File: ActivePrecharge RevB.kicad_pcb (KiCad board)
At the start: 2 copper layers, 98.4 x 58.9 mm, 78 parts, among them IC1 AMC1350DWVR, IC2 AMC1350DWVR, IC4 MCP6496UT-E_LT, IC5 MCP6496UT-E_LT, J1 HVConnector, J2 ExportConnector, J3 PrechargeContactor, J4 MainContactor, J5 Conn_01x07_Pin, U1 LT1963AEST-3.3#TRPBF

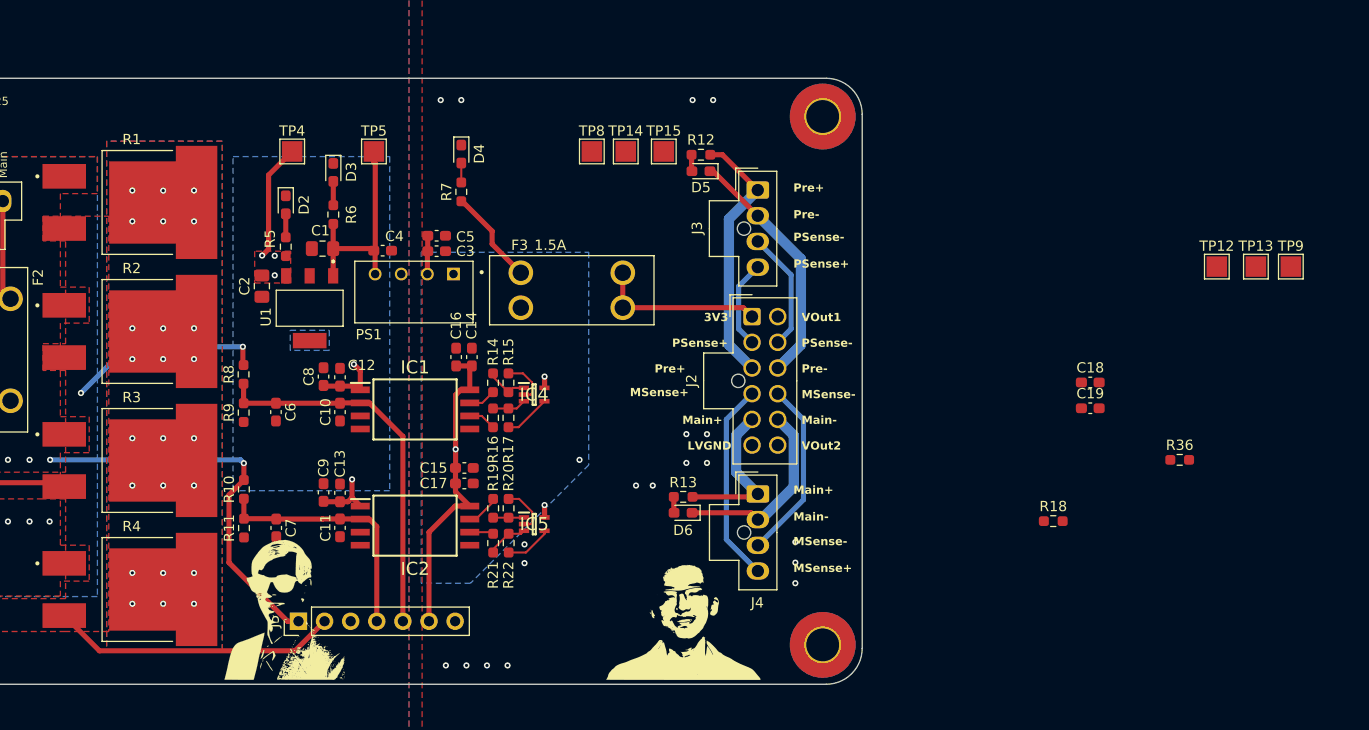
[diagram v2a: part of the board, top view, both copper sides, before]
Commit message: Did some of the initial layout after schematic changes, concerned about the choking on how i currently have the opamp kind of set up, also havent touched the testpoints yet so that will probably make it more complex
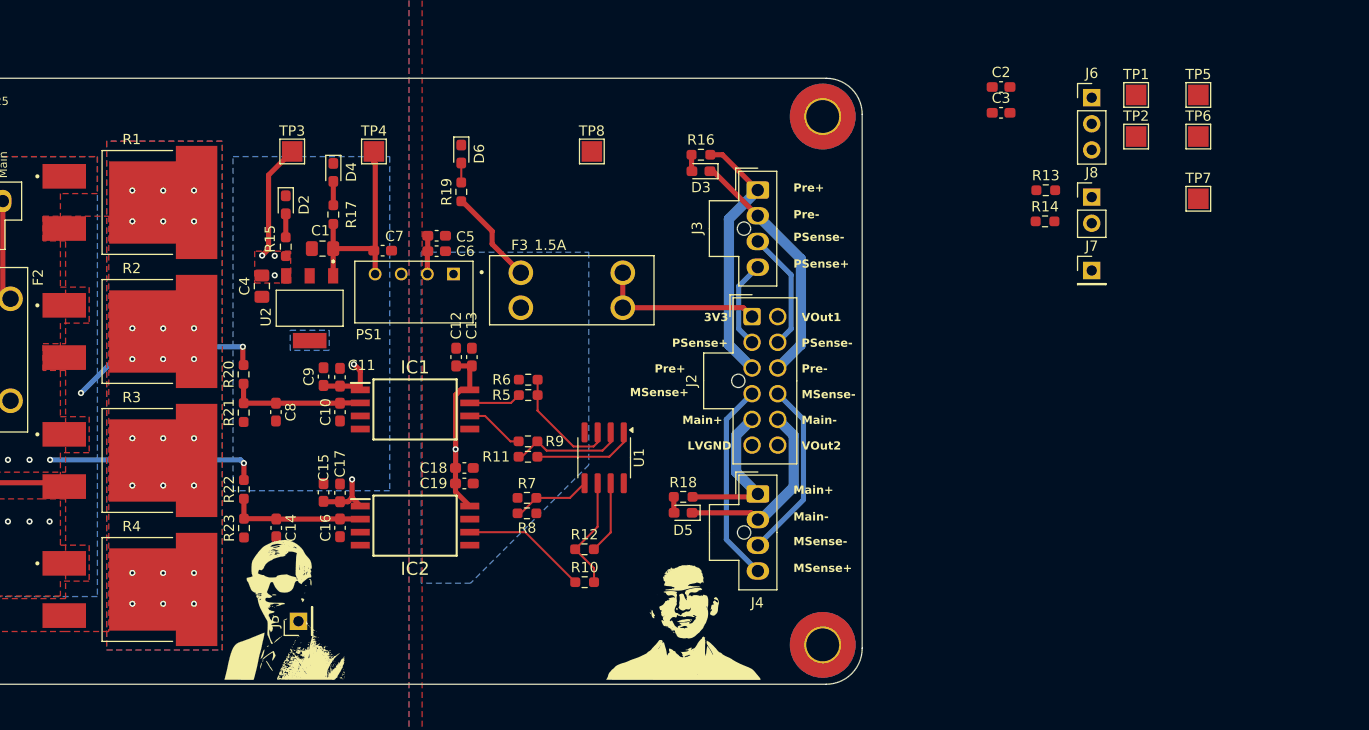
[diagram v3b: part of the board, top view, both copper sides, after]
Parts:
- removed the C18 at (220.7, 89.5)
- removed the C19 at (220.7, 92.0)
- removed IC4, IC5: MCP6496UT-E_LT, ActivePrecharge-RevB:SOT65P210X110-5N
- removed the R15 at (164.1, 89.5)
- removed the R16 at (162.6, 92.9)
- removed the R17 at (164.1, 92.9)
- removed the R18 at (217.1, 103.0)
- removed the R19 at (162.6, 101.7)
- removed the R20 at (164.1, 101.7)
- removed the R21 at (162.6, 105.1)
- removed the R22 at (164.1, 105.1)
- removed R36: 23, Resistor_SMD:R_0603_1608Metric_Pad0.98x0.95mm_HandSolder
- removed TP12: V1-, TestPoint:TestPoint_Pad_2.0x2.0mm
- removed TP13: V2-, TestPoint:TestPoint_Pad_2.0x2.0mm
- removed TP14: VOut1, TestPoint:TestPoint_Pad_2.0x2.0mm
- removed TP15: VOut2, TestPoint:TestPoint_Pad_2.0x2.0mm
- removed TP9: V2+, TestPoint:TestPoint_Pad_2.0x2.0mm
- added C2: 10nF, Capacitor_SMD:C_0603_1608Metric_Pad1.08x0.95mm_HandSolder, F.Cu at (212.0, 60.7)
- added C3: 10nF, Capacitor_SMD:C_0603_1608Metric_Pad1.08x0.95mm_HandSolder, F.Cu at (212.0, 63.2)
- added J6: Conn_01x03_Pin, Connector_PinHeader_2.54mm:PinHeader_1x03_P2.54mm_Vertical, F.Cu at (220.8, 61.8)
- added J7: Conn_01x01_Pin, Connector_PinHeader_2.54mm:PinHeader_1x01_P2.54mm_Vertical, F.Cu at (220.8, 78.6)
- added J8: Conn_01x02_Pin, Connector_PinHeader_2.54mm:PinHeader_1x02_P2.54mm_Vertical, F.Cu at (220.8, 71.4)
- added R10: 10k, Resistor_SMD:R_0603_1608Metric_Pad0.98x0.95mm_HandSolder, F.Cu at (171.5, 108.9)
- added R11: 10k, Resistor_SMD:R_0603_1608Metric_Pad0.98x0.95mm_HandSolder, F.Cu at (166.0, 96.7)
- added R12: 10k, Resistor_SMD:R_0603_1608Metric_Pad0.98x0.95mm_HandSolder, F.Cu at (171.5, 105.7)
- added R13: 10, Resistor_SMD:R_0603_1608Metric_Pad0.98x0.95mm_HandSolder, F.Cu at (216.4, 70.8)
- added R5: 10k, Resistor_SMD:R_0603_1608Metric_Pad0.98x0.95mm_HandSolder, F.Cu at (166.0, 90.7)
- added R6: 10k, Resistor_SMD:R_0603_1608Metric_Pad0.98x0.95mm_HandSolder, F.Cu at (166.0, 89.2)
- added R7: 10k, Resistor_SMD:R_0603_1608Metric_Pad0.98x0.95mm_HandSolder, F.Cu at (165.9, 100.7)
- added R8: 10k, Resistor_SMD:R_0603_1608Metric_Pad0.98x0.95mm_HandSolder, F.Cu at (165.9, 102.2)
- added R9: 10k, Resistor_SMD:R_0603_1608Metric_Pad0.98x0.95mm_HandSolder, F.Cu at (166.0, 95.2)
- added TP1: VOut1, TestPoint:TestPoint_Pad_2.0x2.0mm, F.Cu at (225.2, 61.5)
- added TP2: VOut2, TestPoint:TestPoint_Pad_2.0x2.0mm, F.Cu at (225.2, 65.5)
- added TP5: V+, TestPoint:TestPoint_Pad_2.0x2.0mm, F.Cu at (231.2, 61.5)
- added TP6: V-, TestPoint:TestPoint_Pad_2.0x2.0mm, F.Cu at (231.2, 65.5)
- added TP7: V+, TestPoint:TestPoint_Pad_2.0x2.0mm, F.Cu at (231.2, 71.6)
- added U1: TLV9002QDRQ1, Package_SO:SOIC-8_3.9x4.9mm_P1.27mm, F.Cu at (173.4, 96.8)
- C12: renamed from C16; value 100nF -> 1uF
- C13: renamed from C14; value 1uF -> 100nF
- J5: value Conn_01x07_Pin -> Conn_01x01_Pin; footprint Connector_PinHeader_2.54mm:PinHeader_1x07_P2.54mm_Vertical -> Connector_PinHeader_2.54mm:PinHeader_1x01_P2.54mm_Vertical
- R14: value 20k -> 10
- R16: renamed from R12; value 1k -> 10k
- R18: renamed from R13; value 1k -> 10k
- TP8: value V1+ -> V-
- moved R14 55.9 mm to (216.3, 73.8), turned to 0 degrees
- renumbered C12 to C11, C7 to C14, C9 to C15, C11 to C16, C13 to C17, C15 to C18, C17 to C19, C2 to C4, C3 to C6, C4 to C7, C6 to C8, C8 to C9, D5 to D3, D3 to D4, D6 to D5, D4 to D6, R5 to R15, R6 to R17, R7 to R19, R8 to R20, R9 to R21, R10 to R22, R11 to R23, TP4 to TP3, TP5 to TP4, U1 to U2
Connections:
- C10 pad 1: /Voltage_Sense/Vin1 -> /Vin1
- C14 pad 1: /Voltage_Sense/Vin2 -> /Vin2
- C16 pad 1: /Voltage_Sense/Vin2 -> /Vin2
- C8 pad 1: /Voltage_Sense/Vin1 -> /Vin1
- IC1 pad 2: /Voltage_Sense/Vin1 -> /Vin1
- IC1 pad 6: /Voltage_Sense/V1- -> /V1-
- IC1 pad 7: /Voltage_Sense/V1+ -> /V1+
- IC2 pad 2: /Voltage_Sense/Vin2 -> /Vin2
- IC2 pad 6: /Voltage_Sense/V2- -> /V2-
- IC2 pad 7: /Voltage_Sense/V2+ -> /V2+
- J5 pad 1: HV- -> HV+
- R14 pad 1: Net-(IC4-VIN+) -> /VOut2
- R14 pad 2: /Voltage_Sense/V1+ -> Net-(R12-Pad2)
- R20 pad 1: /Voltage_Sense/Vin1 -> /Vin1
- R21 pad 2: /Voltage_Sense/Vin1 -> /Vin1
- R22 pad 1: /Voltage_Sense/Vin2 -> /Vin2
- R23 pad 2: /Voltage_Sense/Vin2 -> /Vin2
- TP8 pad 1: /Voltage_Sense/V1+ -> /V2-
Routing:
- net /Voltage_Sense/Vin1: track 36.7 -> 0.00 mm
- net HV+: track 62.1 -> 34.1 mm
- net /Voltage_Sense/Vin2: track 24.4 -> 0.00 mm
- net HV-: track 42.7 -> 25.0 mm
- net 3V3: track 46.1 -> 30.1 mm, vias 3 -> 1
- net /Vin2: track 0.00 -> 13.3 mm
- net /Vin1: track 0.00 -> 13.3 mm
- net /V2-: track 0.00 -> 12.3 mm
- net Net-(U1A-+): track 0.00 -> 11.4 mm
- net Net-(U1B--): track 0.00 -> 11.3 mm
- net Net-(U1A--): track 0.00 -> 11.3 mm
- net Net-(R11-Pad1): track 0.00 -> 9.96 mm
- net LVGND: track 9.31 -> 0.00 mm, vias 21 -> 0
- net Net-(U1B-+): track 0.00 -> 7.73 mm
- net Net-(R12-Pad2): track 0.00 -> 7.10 mm
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
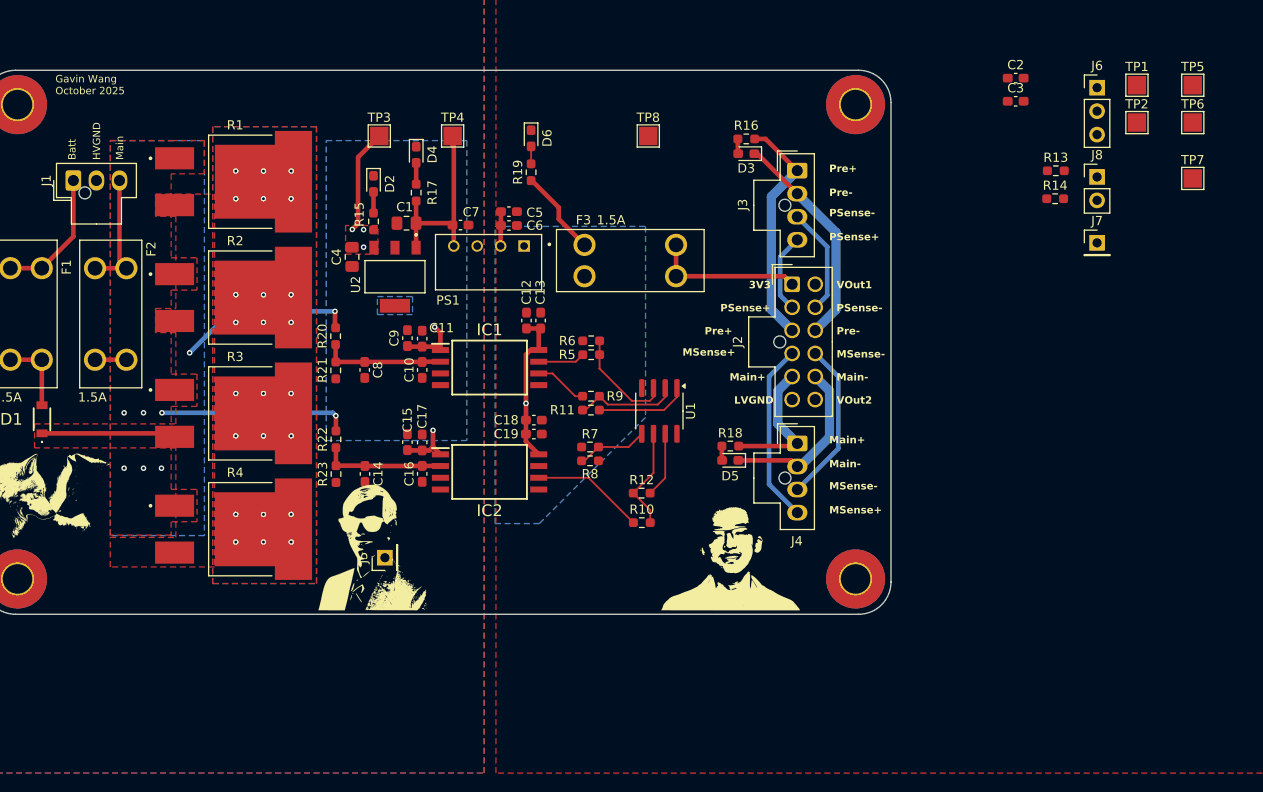
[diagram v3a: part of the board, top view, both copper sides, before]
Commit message: First draft of the layout is complete, I think its workable rn but the vias might need a little work
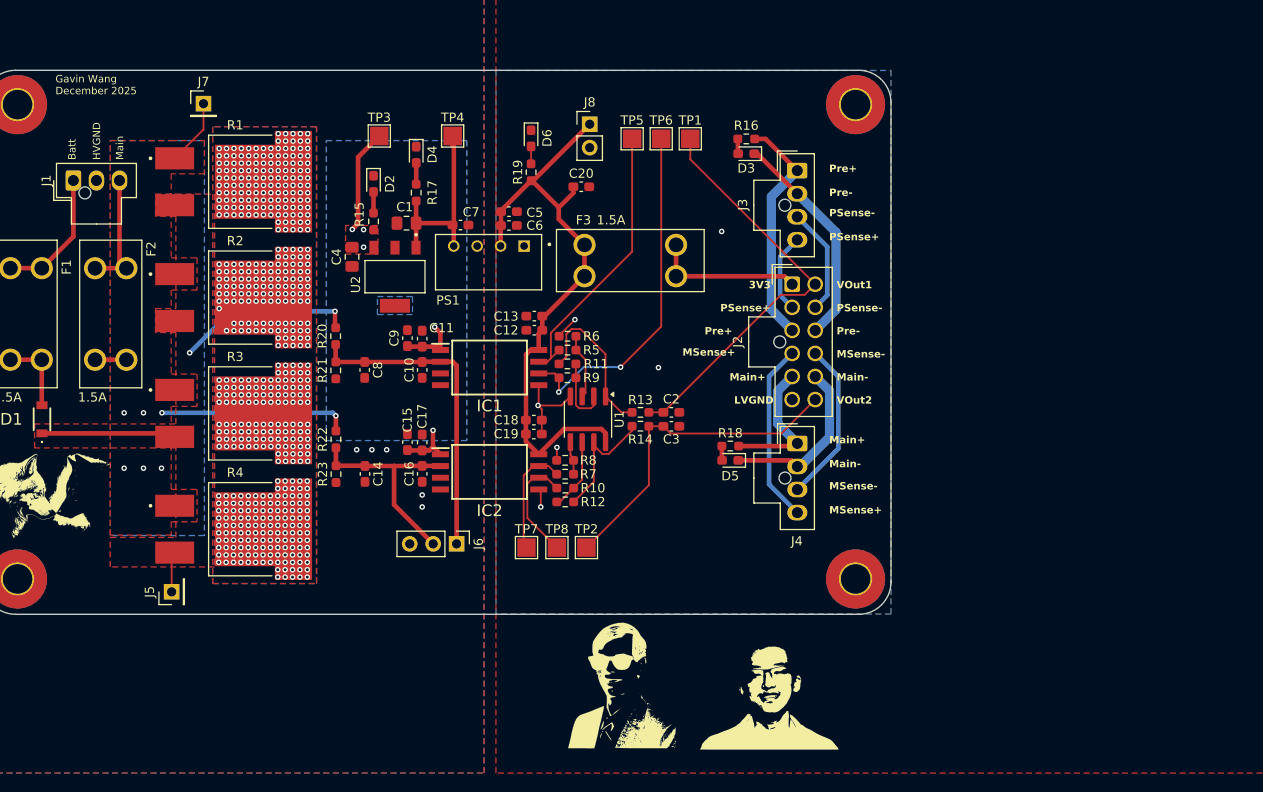
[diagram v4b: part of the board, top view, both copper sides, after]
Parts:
- added C20: 1uF, Capacitor_SMD:C_0603_1608Metric_Pad1.08x0.95mm_HandSolder, F.Cu at (164.9, 72.5)
- moved J7 98.0 mm to (124.0, 63.5)
- moved J6 85.2 mm to (151.4, 111.2), turned to -90 degrees
- moved TP7 82.5 mm to (159.0, 111.6)
- moved TP2 75.4 mm to (165.5, 111.6)
- moved TP5 61.0 mm to (170.4, 67.3)
- moved TP6 57.6 mm to (173.6, 67.3)
- moved J8 55.3 mm to (165.8, 65.7)
- moved R13 52.1 mm to (171.3, 97.0), turned to 180 degrees
- moved C2 52.0 mm to (174.7, 97.0)
- moved C3 51.3 mm to (174.7, 98.5)
- moved R14 51.3 mm to (171.3, 98.5), turned to 180 degrees
- moved TP1 48.7 mm to (176.8, 67.3)
- moved TP8 45.7 mm to (162.3, 111.6)
- moved LOGO1 30.9 mm to (168.9, 126.4)
- moved J5 23.4 mm to (120.5, 116.4)
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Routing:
- net /VOut1: track 0.00 -> 45.1 mm
- net /VOut2: track 0.00 -> 35.8 mm
- net 3V3: track 30.1 -> 65.8 mm, vias 1 -> 0
- net /V1-: track 5.77 -> 38.3 mm, vias 0 -> 2
- net /V1+: track 5.09 -> 30.2 mm
- net /Vin1: track 13.3 -> 34.5 mm
- net LVGND: track 0.00 -> 15.3 mm, vias 0 -> 6
- net /V2+: track 0.00 -> 12.3 mm
- net /Vin2: track 13.3 -> 23.5 mm
- net Net-(R11-Pad1): track 9.96 -> 17.3 mm
- net HV-: track 25.0 -> 32.2 mm
- net Net-(R12-Pad2): track 7.10 -> 13.8 mm
- net HV+: track 34.1 -> 38.5 mm
- net Net-(U1A-+): track 11.4 -> 7.11 mm
- net Net-(U1B-+): track 7.73 -> 3.62 mm
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- added copper zone on B.Cu, net LVGND
- removed copper zone on B.Cu, net 3V3
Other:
- board text added: "Gavin Wang December 2025"
- board text removed: "Gavin Wang October 2025"

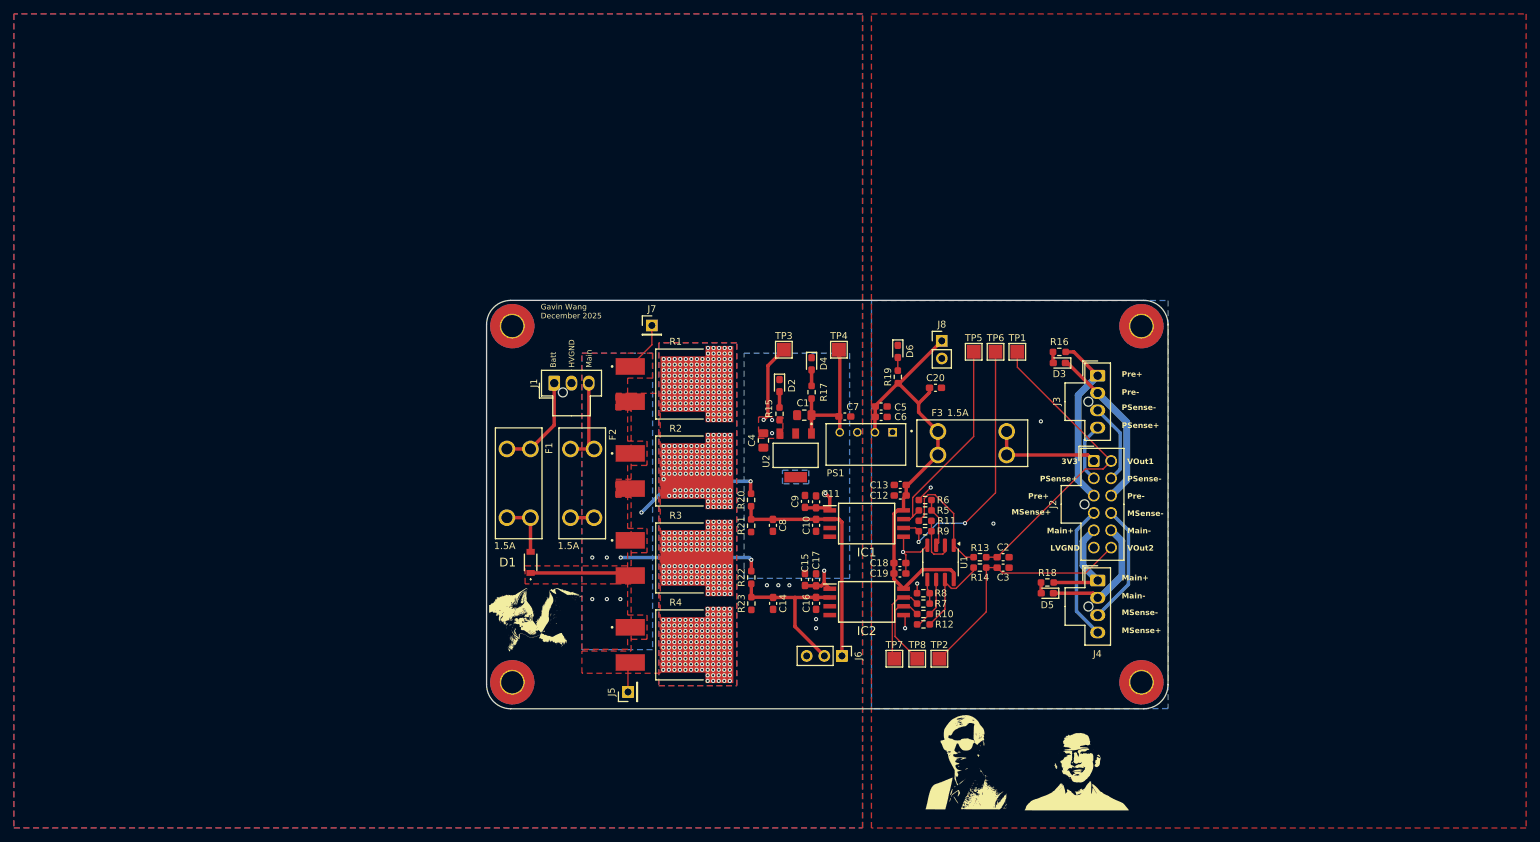
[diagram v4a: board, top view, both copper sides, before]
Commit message: Addressed most things, still need to add more stitching vias, flybacks, change testpoints, and compact everything some more
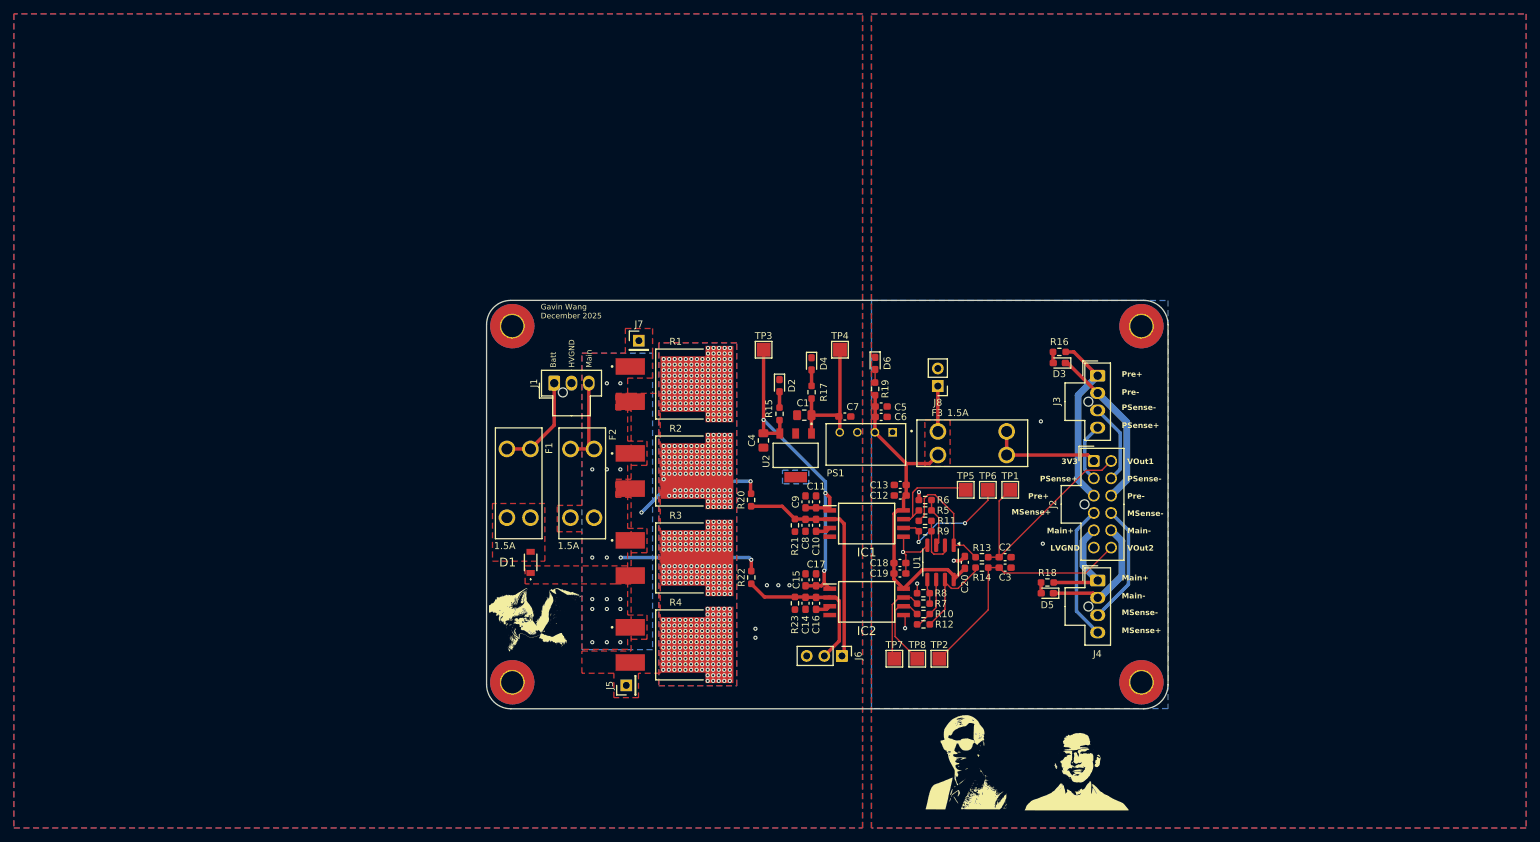
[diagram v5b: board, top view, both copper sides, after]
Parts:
- moved C20 25.6 mm to (169.2, 97.7), turned to 90 degrees
- moved TP5 20.0 mm to (169.3, 87.2)
- moved TP6 20.0 mm to (172.5, 87.2)
- moved TP1 20.0 mm to (175.7, 87.2)
- moved LOGO2 18.0 mm to (132.9, 62.4)
- moved J8 6.55 mm to (165.3, 72.2), turned to 180 degrees
- moved R21 6.32 mm to (144.7, 92.3)
- moved R23 6.29 mm to (144.7, 103.6)
- moved C8 4.71 mm to (146.2, 92.3)
- moved C14 4.68 mm to (146.2, 103.6)
- moved D6 3.70 mm to (156.2, 69.0)
- moved R19 3.70 mm to (156.2, 72.7)
- moved TP3 2.93 mm to (140.1, 67.0)
- moved J7 2.89 mm to (122.1, 65.7)
- moved J5 0.98 mm to (120.3, 115.5)
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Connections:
- net Net-(D1-A) renamed /HV+_Fused
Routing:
- net REG_3V3: track 24.1 -> 54.4 mm, vias 5 -> 3
- net /V1-: track 38.3 -> 18.0 mm
- net HV+: track 38.5 -> 19.6 mm
- net /V1+: track 30.2 -> 14.3 mm
- net /VOut1: track 45.1 -> 33.9 mm
- net 3V3: track 65.8 -> 54.9 mm
- net HV-: track 32.2 -> 21.6 mm, vias 7 -> 18
- net /HV+_Fused: track 8.34 -> 0.00 mm
- net HVGND: track 0.00 -> 4.33 mm
- net /Vin2: track 23.5 -> 22.6 mm
- net /Vin1: track 34.5 -> 33.7 mm
- net LVGND: track 15.3 -> 15.8 mm, vias 6 -> 7
- added copper zone on F.Cu, net /HV+_Fused
- added copper zone on F.Cu, net 3V3
- removed copper zone on B.Cu, net REG_3V3
- removed copper zone on F.Cu, net REG_3V3
